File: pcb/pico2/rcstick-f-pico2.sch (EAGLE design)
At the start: 42 parts, among them J1 USB-TYPEC-1054440001-HS, J2 2212S, SW1 SKRPACE010, U1 STM32F042K6U6, U2 CC2500, U3 MCP1703AT-3302E/CB, X1 16MHz/10pF, X2 26MHz/9pF, X3 (50 Ohm)

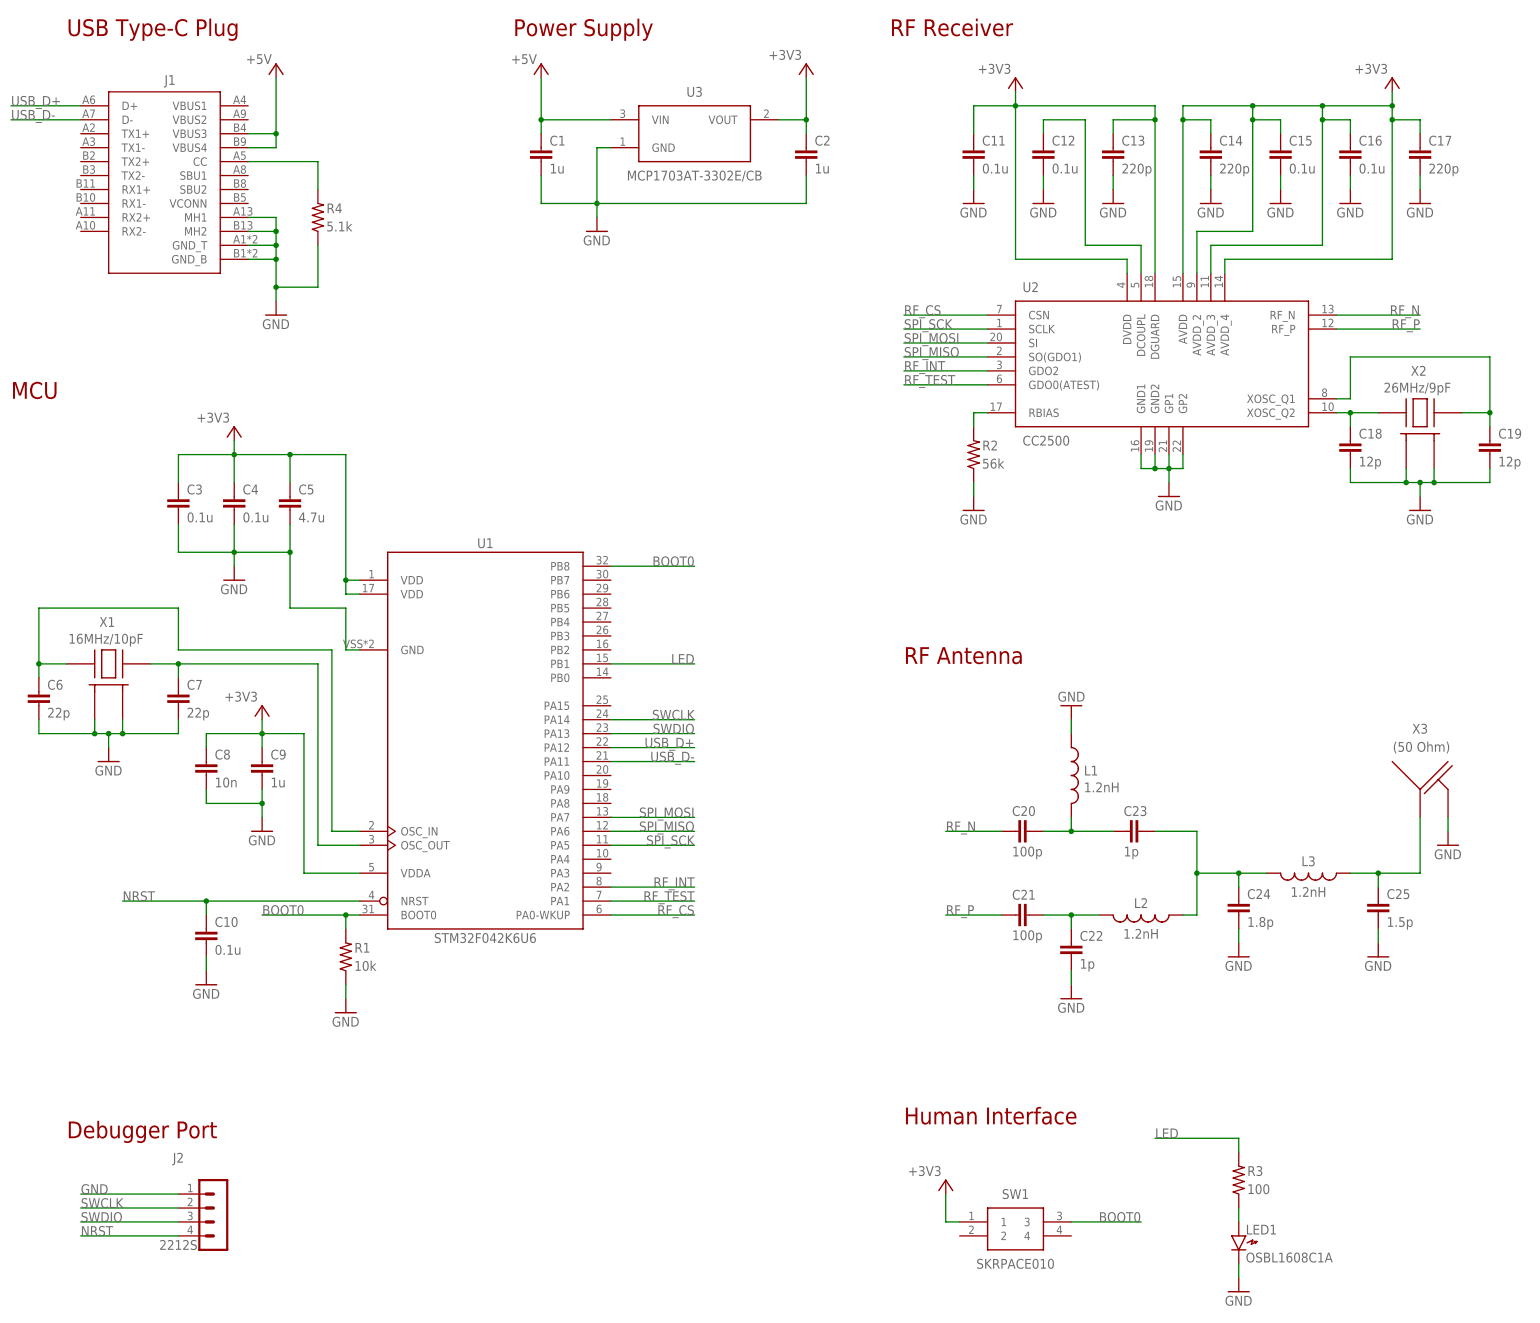
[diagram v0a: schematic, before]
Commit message: added QFN28 MCU version
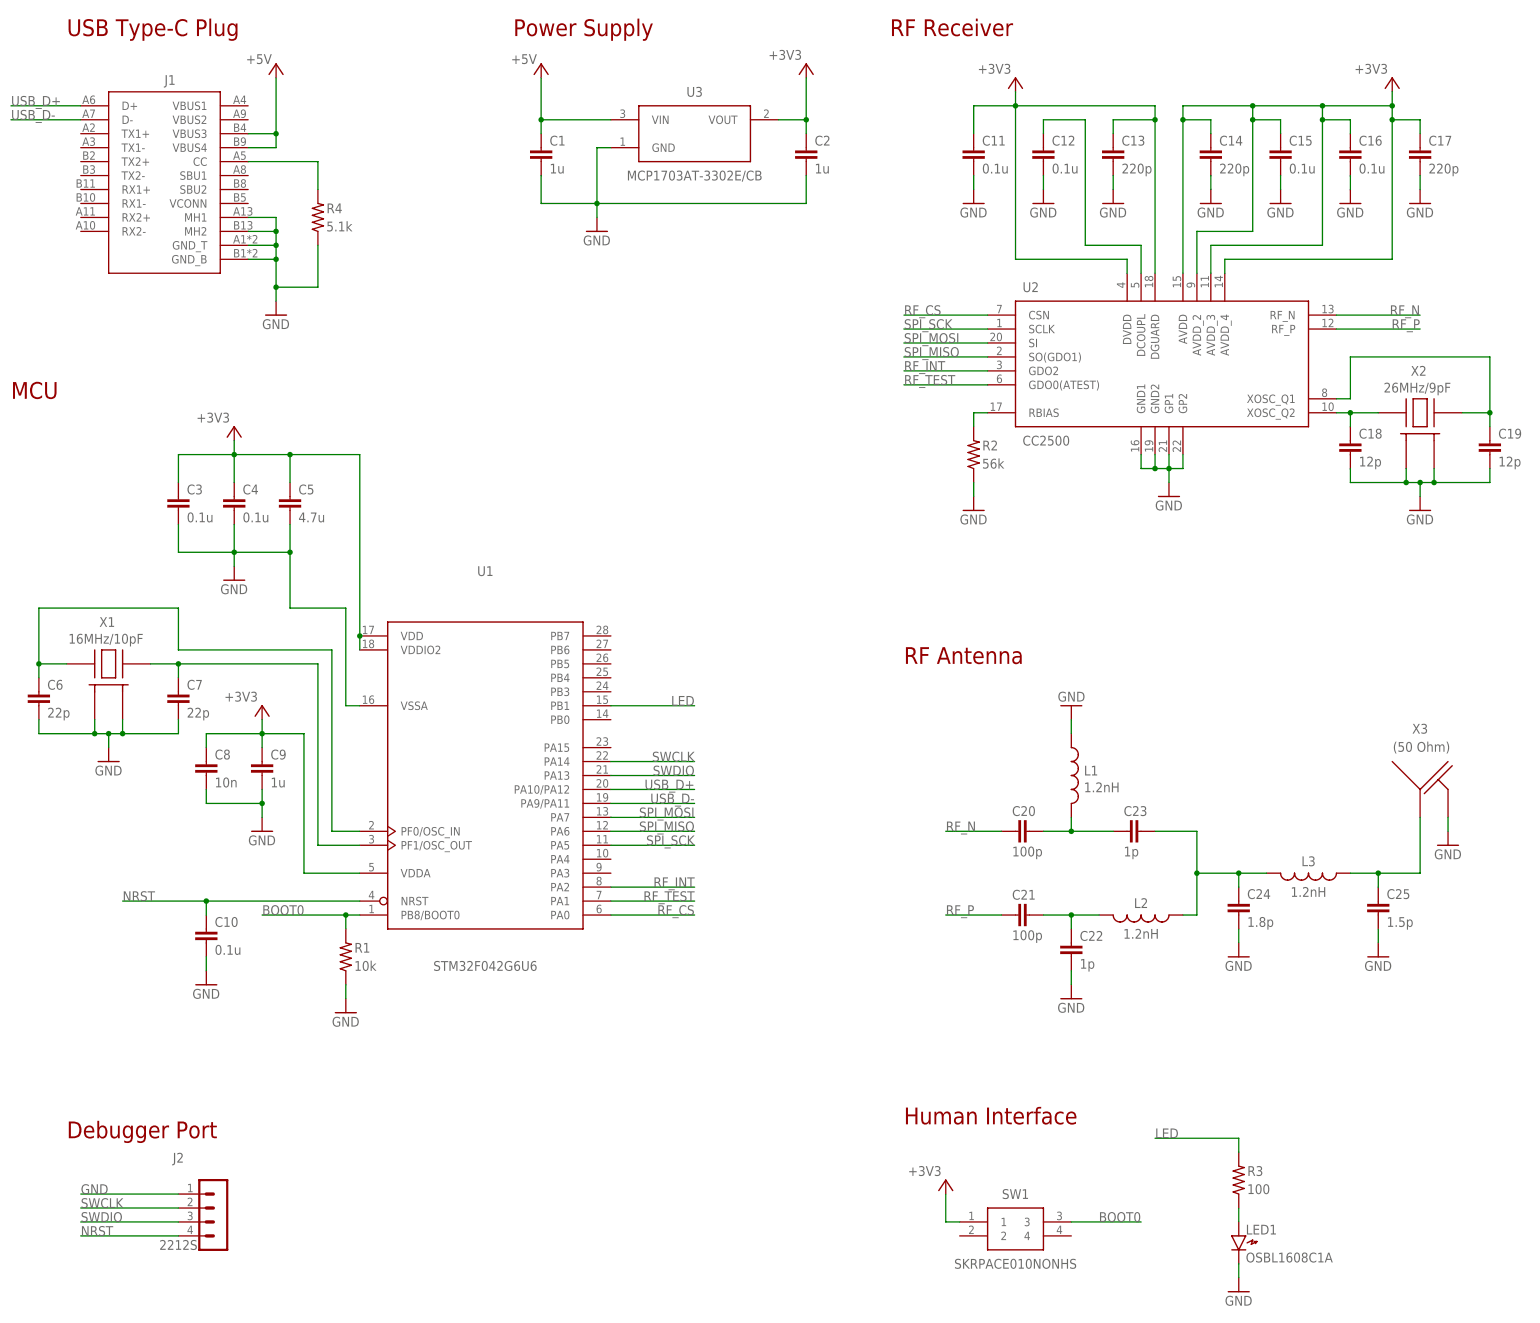
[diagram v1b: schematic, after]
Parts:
- LED1: device gen-discrete:LED1608 -> gen-discrete:LED1608_NOHS
- SW1: value SKRPACE010 -> SKRPACE010NONHS; device SKRPACE010:SKRPACE010 -> SKRPACE010:SKRPACE010NONHS
- U1: value STM32F042K6U6 -> STM32F042G6U6; device stm32:STM32F042K6U-M -> stm32:STM32F042GU
- U2: device CC2500:CC2500-HS -> CC2500:CC2500
- U3: device SOT23_Module:LDO-REGULATOR -> SOT23_Module:LDO-REGULATOR_NOHS
- X1, X2: device CRYSTAL3225:CRYSTAL3225HS -> CRYSTAL3225:CRYSTAL3225
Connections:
- net +3V3: now also U1.VDD, U1.VDDIO2; no longer U1.VDD@1, U1.VDD@2
- net BOOT0: now also U1.PB8/BOOT0; no longer U1.BOOT0, U1.PB8
- net GND: now also U1.VSSA; no longer U1.GND
- net OSC_IN: now also U1.PF0/OSC_IN; no longer U1.OSC_IN
- net OSC_OUT: now also U1.PF1/OSC_OUT; no longer U1.OSC_OUT
- net RF_CS: now also U1.PA0; no longer U1.PA0-WKUP
- net USB_D+: now also U1.PA10/PA12; no longer U1.PA12
- net USB_D-: now also U1.PA9/PA11; no longer U1.PA11
